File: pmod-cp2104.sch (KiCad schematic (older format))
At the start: 41 parts, among them P1 PMOD-CONN_6X2, P2 USB_OTG, SW1 SW_PUSH, U1 CP2104

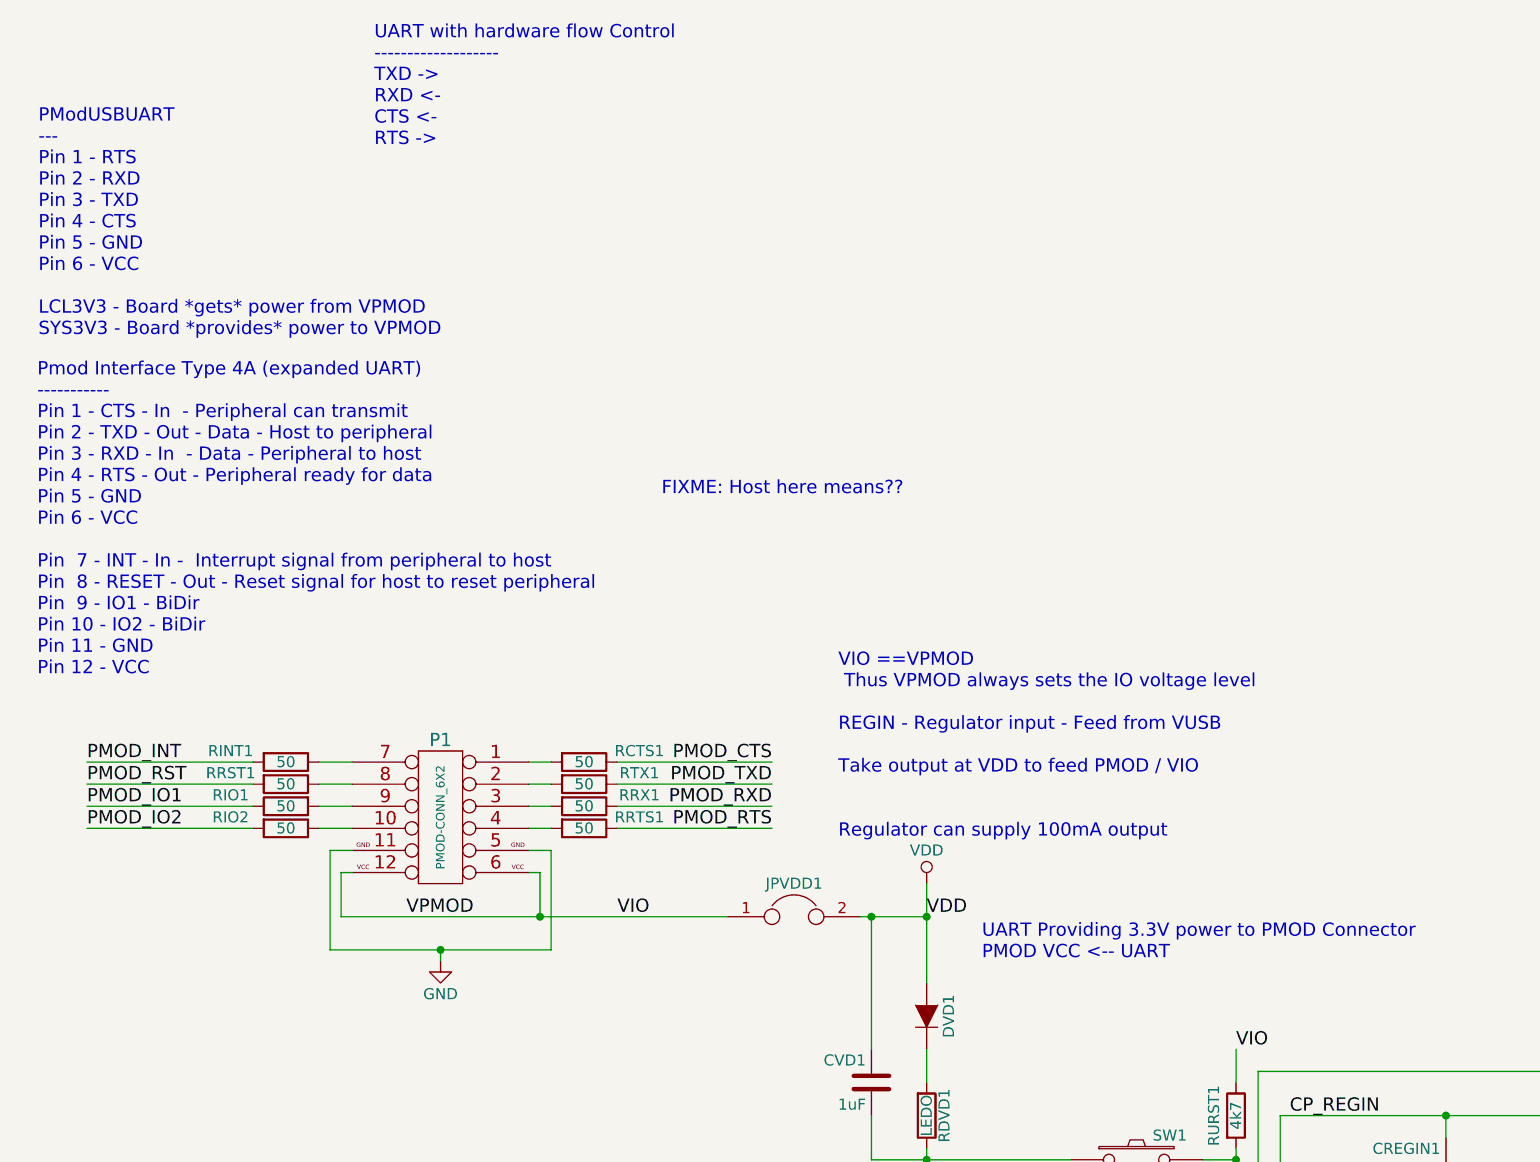
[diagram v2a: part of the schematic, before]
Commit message: Changing to using the pmod library.
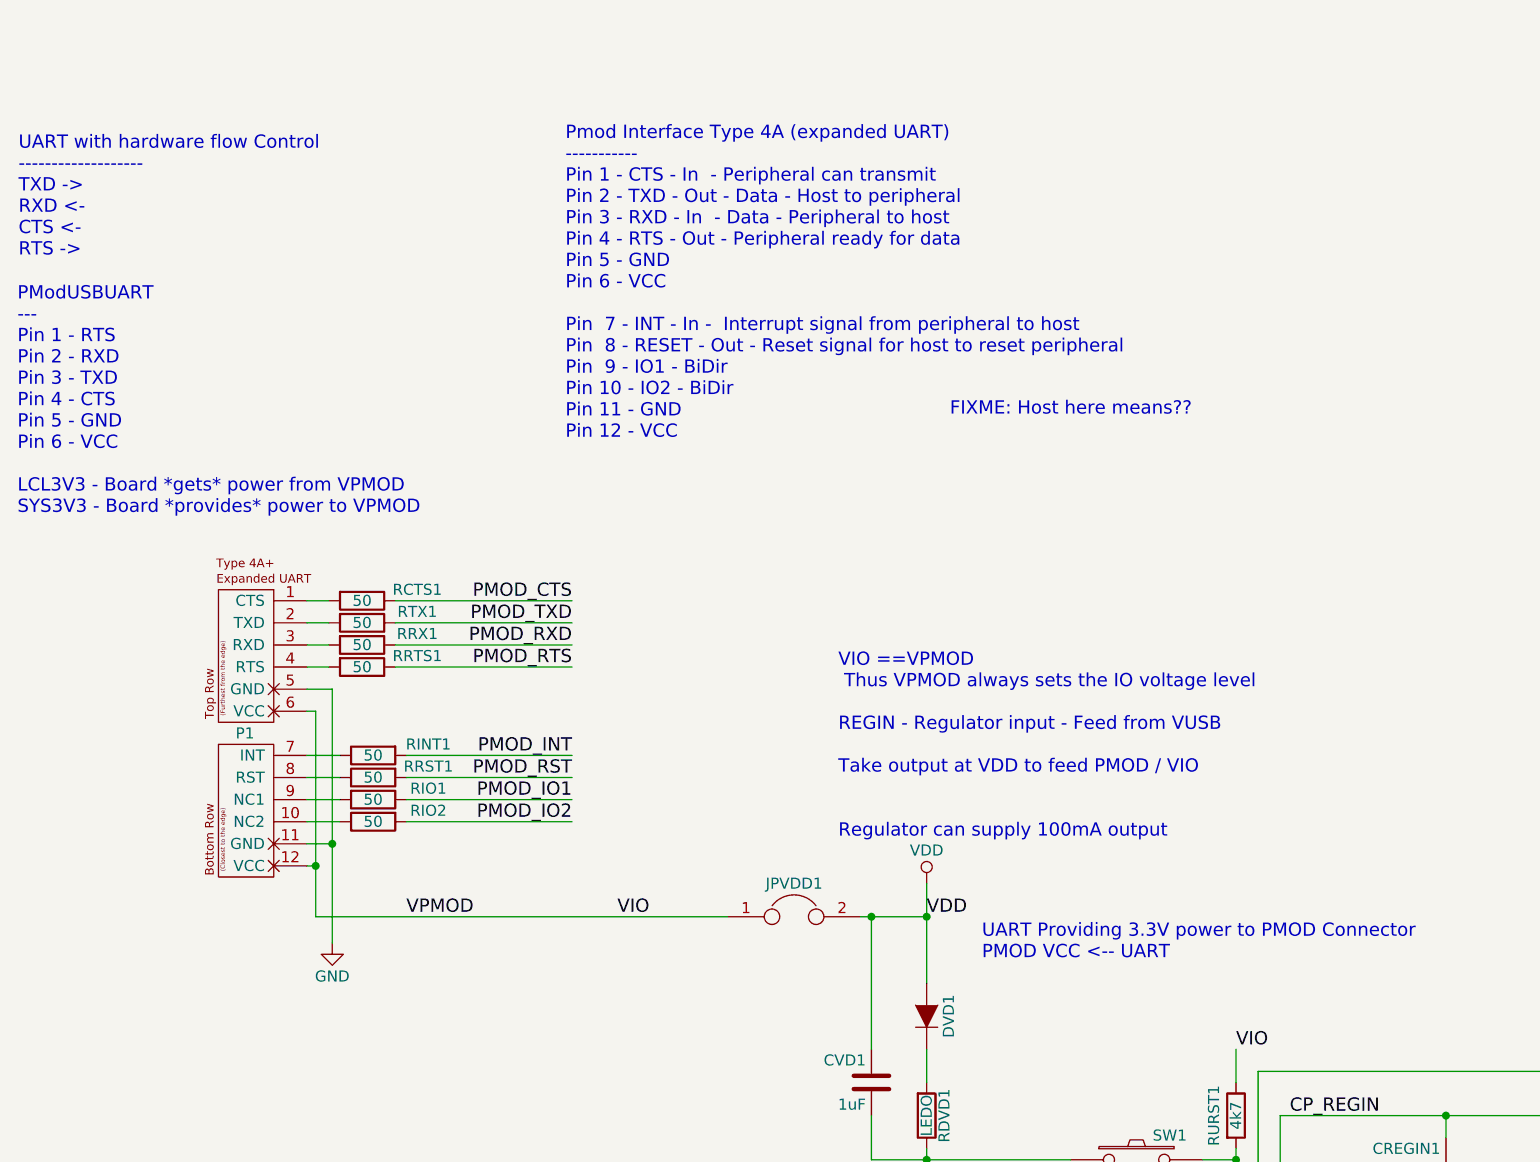
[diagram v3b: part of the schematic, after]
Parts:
- removed P1: PMOD-CONN_6X2, Pin_Headers:Pin_Header_Angled_2x06, symbol PMOD-CONN_6X2
- added P1: PMOD-Device-x2-Type-4A+-Expanded-UART, pmod-conn_6x2:pmod_pin_array_6x2, symbol PMOD-Device-x2-Type-4A+-Expanded-UART
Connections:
- net GND: now also P1.11 (GND), P1.5 (GND)
- net VIO: now also P1.12 (VCC), P1.6 (VCC)
- net at RCTS1.2: now also P1.1 (CTS)
- net at RIO2.1: now also P1.10 (NC2)
- net at RTX1.2: now also P1.2 (TXD)
- net at RRX1.2: now also P1.3 (RXD)
- net at RRTS1.2: now also P1.4 (RTS)
- net at RINT1.1: now also P1.7 (INT)
- net at RRST1.1: now also P1.8 (RST)
- net at RIO1.2: now also P1.9 (NC1)
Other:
- moved on the sheet: RCTS1, RINT1, RIO1, RIO2, RRST1, RRTS1, RRX1, RTX1
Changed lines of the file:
@@
 LIBS:contrib
 LIBS:valves
-LIBS:pmod-conn_6x2
 LIBS:cp2104
+LIBS:pmod
 LIBS:pmod-cp2104-cache
 EELAYER 25 0
@@
 Comment4 ""
 $EndDescr
-$Comp
-L PMOD-CONN_6X2 P1
-U 1 1 57F4CF0B
-P 2690 4475
-F 0 "P1" H 2690 4825 60  0000 C CNN
-F 1 "PMOD-CONN_6X2" V 2690 4475 39  0000 C CNN
-F 2 "Pin_Headers:Pin_Header_Angled_2x06" H 2690 4475 60  0001 C CNN
-F 3 "" H 2690 4475 60  0000 C CNN
-	1    2690 4475
-	-1   0    0    -1
-$EndComp
-Text Notes 2390 1445 0    60   ~ 0
+Text Notes 780  1945 0    60   ~ 0
 UART with hardware flow Control\n-------------------\nTXD ->\nRXD <-\nCTS <-\nRTS ->\n
 $Comp
@@
 	1    0    0    1
 $EndComp
-Text Notes 865  3840 0    60   ~ 0
+Text Notes 3255 2770 0    60   ~ 0
 Pmod Interface Type 4A (expanded UART) \n-----------\nPin 1 - CTS - In  - Peripheral can transmit\nPin 2 - TXD - Out - Data - Host to peripheral\nPin 3 - RXD - In  - Data - Peripheral to host\nPin 4 - RTS - Out - Peripheral ready for data\nPin 5 - GND\nPin 6 - VCC\n\nPin  7 - INT - In -  Interrupt signal from peripheral to host \nPin  8 - RESET - Out - Reset signal for host to reset peripheral \nPin  9 - IO1 - BiDir\nPin 10 - IO2 - BiDir\nPin 11 - GND\nPin 12 - VCC
-Text Label 4190 4225 2    60   ~ 0
+Text Label 3285 3495 2    60   ~ 0
 PMOD_CTS
-Text Label 4190 4325 2    60   ~ 0
+Text Label 3285 3595 2    60   ~ 0
 PMOD_TXD
-Text Label 4190 4425 2    60   ~ 0
+Text Label 3285 3695 2    60   ~ 0
 PMOD_RXD
-Text Label 4190 4525 2    60   ~ 0
+Text Label 3285 3795 2    60   ~ 0
 PMOD_RTS
-Text Label 1090 4225 0    60   ~ 0
+Text Label 3285 4195 2    60   ~ 0
 PMOD_INT
-Text Label 1090 4325 0    60   ~ 0
+Text Label 3285 4295 2    60   ~ 0
 PMOD_RST
-Text Label 1090 4425 0    60   ~ 0
+Text Label 3285 4395 2    60   ~ 0
 PMOD_IO1
-Text Label 1090 4525 0    60   ~ 0
+Text Label 3285 4495 2    60   ~ 0
 PMOD_IO2
 Text Label 8390 7225 0    60   ~ 0
@@
 L GND #PWR01
 U 1 1 57F4D651
-P 2690 5125
-F 0 "#PWR01" H 2690 4875 50  0001 C CNN
-F 1 "GND" H 2690 4975 50  0000 C CNN
-F 2 "" H 2690 5125 50  0000 C CNN
-F 3 "" H 2690 5125 50  0000 C CNN
-	1    2690 5125
+P 2200 5045
+F 0 "#PWR01" H 2200 4795 50  0001 C CNN
+F 1 "GND" H 2200 4895 50  0000 C CNN
+F 2 "" H 2200 5045 50  0000 C CNN
+F 3 "" H 2200 5045 50  0000 C CNN
+	1    2200 5045
 	-1   0    0    -1
 $EndComp
@@
 	1    0    0    -1
 $EndComp
-Text Notes 870  2305 0    60   ~ 0
+Text Notes 775  3110 0    60   ~ 0
 PModUSBUART\n---\nPin 1 - RTS\nPin 2 - RXD\nPin 3 - TXD\nPin 4 - CTS\nPin 5 - GND\nPin 6 - VCC\n\nLCL3V3 - Board *gets* power from VPMOD\nSYS3V3 - Board *provides* power to VPMOD
 Text Notes 4490 4575 0    60   ~ 0
@@
 L R RINT1
 U 1 1 57F500C7
-P 1990 4225
-F 0 "RINT1" V 1940 3975 50  0000 C CNN
-F 1 "50" V 1990 4225 50  0000 C CNN
-F 2 "Resistors_SMD:R_0603" V 1920 4225 50  0001 C CNN
-F 3 "" H 1990 4225 50  0000 C CNN
-	1    1990 4225
-	0    1    1    0
+P 2385 4195
+F 0 "RINT1" V 2335 3945 50  0000 C CNN
+F 1 "50" V 2385 4195 50  0000 C CNN
+F 2 "Resistors_SMD:R_0603" V 2315 4195 50  0001 C CNN
+F 3 "" H 2385 4195 50  0000 C CNN
+	1    2385 4195
+	0    -1   1    0
 $EndComp
 Text Label 11065 8015 0    60   ~ 0
@@
 L R RRST1
 U 1 1 57F52EB3
-P 1990 4325
-F 0 "RRST1" V 1940 4075 50  0000 C CNN
-F 1 "50" V 1990 4325 50  0000 C CNN
-F 2 "Resistors_SMD:R_0603" V 1920 4325 50  0001 C CNN
-F 3 "" H 1990 4325 50  0000 C CNN
-	1    1990 4325
-	0    1    1    0
+P 2385 4295
+F 0 "RRST1" V 2335 4045 50  0000 C CNN
+F 1 "50" V 2385 4295 50  0000 C CNN
+F 2 "Resistors_SMD:R_0603" V 2315 4295 50  0001 C CNN
+F 3 "" H 2385 4295 50  0000 C CNN
+	1    2385 4295
+	0    -1   1    0
 $EndComp
 $Comp
 L R RIO2
 U 1 1 57F53D72
-P 1990 4525
-F 0 "RIO2" V 1940 4275 50  0000 C CNN
-F 1 "50" V 1990 4525 50  0000 C CNN
-F 2 "Resistors_SMD:R_0603" V 1920 4525 50  0001 C CNN
-F 3 "" H 1990 4525 50  0000 C CNN
-	1    1990 4525
-	0    1    1    0
+P 2385 4495
+F 0 "RIO2" V 2335 4245 50  0000 C CNN
+F 1 "50" V 2385 4495 50  0000 C CNN
+F 2 "Resistors_SMD:R_0603" V 2315 4495 50  0001 C CNN
+F 3 "" H 2385 4495 50  0000 C CNN
+	1    2385 4495
+	0    -1   1    0
 $EndComp
 $Comp
 L R RTX1
 U 1 1 57F54253
-P 3340 4325
-F 0 "RTX1" V 3290 4575 50  0000 C CNN
-F 1 "50" V 3340 4325 50  0000 C CNN
-F 2 "Resistors_SMD:R_0603" V 3270 4325 50  0001 C CNN
-F 3 "" H 3340 4325 50  0000 C CNN
-	1    3340 4325
+P 2335 3595
+F 0 "RTX1" V 2285 3845 50  0000 C CNN
+F 1 "50" V 2335 3595 50  0000 C CNN
+F 2 "Resistors_SMD:R_0603" V 2265 3595 50  0001 C CNN
+F 3 "" H 2335 3595 50  0000 C CNN
+	1    2335 3595
 	0    1    1    0
 $EndComp
@@
 L R RRX1
 U 1 1 57F543D4
-P 3340 4425
-F 0 "RRX1" V 3290 4675 50  0000 C CNN
-F 1 "50" V 3340 4425 50  0000 C CNN
-F 2 "Resistors_SMD:R_0603" V 3270 4425 50  0001 C CNN
-F 3 "" H 3340 4425 50  0000 C CNN
-	1    3340 4425
+P 2335 3695
+F 0 "RRX1" V 2285 3945 50  0000 C CNN
+F 1 "50" V 2335 3695 50  0000 C CNN
+F 2 "Resistors_SMD:R_0603" V 2265 3695 50  0001 C CNN
+F 3 "" H 2335 3695 50  0000 C CNN
+	1    2335 3695
 	0    1    1    0
 $EndComp
@@
 L R RCTS1
 U 1 1 57F54490
-P 3340 4225
-F 0 "RCTS1" V 3290 4475 50  0000 C CNN
-F 1 "50" V 3340 4225 50  0000 C CNN
-F 2 "Resistors_SMD:R_0603" V 3270 4225 50  0001 C CNN
-F 3 "" H 3340 4225 50  0000 C CNN
-	1    3340 4225
+P 2335 3495
+F 0 "RCTS1" V 2285 3745 50  0000 C CNN
+F 1 "50" V 2335 3495 50  0000 C CNN
+F 2 "Resistors_SMD:R_0603" V 2265 3495 50  0001 C CNN
+F 3 "" H 2335 3495 50  0000 C CNN
+	1    2335 3495
 	0    1    1    0
 $EndComp
@@
 L R RRTS1
 U 1 1 57F545A3
-P 3340 4525
-F 0 "RRTS1" V 3290 4775 50  0000 C CNN
-F 1 "50" V 3340 4525 50  0000 C CNN
-F 2 "Resistors_SMD:R_0603" V 3270 4525 50  0001 C CNN
-F 3 "" H 3340 4525 50  0000 C CNN
-	1    3340 4525
+P 2335 3795
+F 0 "RRTS1" V 2285 4045 50  0000 C CNN
+F 1 "50" V 2335 3795 50  0000 C CNN
+F 2 "Resistors_SMD:R_0603" V 2265 3795 50  0001 C CNN
+F 3 "" H 2335 3795 50  0000 C CNN
+	1    2335 3795
 	0    1    1    0
 $EndComp
@@
 L R RIO1
 U 1 1 57F579B8
-P 1990 4425
-F 0 "RIO1" V 1940 4675 50  0000 C CNN
-F 1 "50" V 1990 4425 50  0000 C CNN
-F 2 "Resistors_SMD:R_0603" V 1920 4425 50  0001 C CNN
-F 3 "" H 1990 4425 50  0000 C CNN
-	1    1990 4425
-	0    -1   1    0
+P 2385 4395
+F 0 "RIO1" V 2335 4645 50  0000 C CNN
+F 1 "50" V 2385 4395 50  0000 C CNN
+F 2 "Resistors_SMD:R_0603" V 2315 4395 50  0001 C CNN
+F 3 "" H 2385 4395 50  0000 C CNN
+	1    2385 4395
+	0    1    1    0
 $EndComp
 $Comp
@@
 $EndComp
 Wire Wire Line
-	2290 4725 2240 4725
-Wire Wire Line
-	2240 4725 2240 4925
-Wire Wire Line
-	2240 4925 3990 4925
-Wire Wire Line
-	3140 4925 3140 4725
-Wire Wire Line
-	3140 4725 3090 4725
-Wire Wire Line
-	3090 4625 3190 4625
-Wire Wire Line
-	3190 4625 3190 5075
-Wire Wire Line
-	3190 5075 2190 5075
-Wire Wire Line
-	2190 5075 2190 4625
-Wire Wire Line
-	2190 4625 2290 4625
-Wire Wire Line
-	2690 5125 2690 5075
-Connection ~ 2690 5075
+	2125 4925 3990 4925
+Wire Wire Line
+	2200 3895 2200 5045
 Wire Wire Line
 	7990 7225 8740 7225
@@
 	12665 4515 12565 4515
 Wire Wire Line
-	3090 4225 3190 4225
-Wire Wire Line
-	3090 4325 3190 4325
-Wire Wire Line
-	3090 4425 3190 4425
-Wire Wire Line
-	3090 4525 3190 4525
-Wire Wire Line
-	3490 4225 4190 4225
-Wire Wire Line
-	4190 4325 3490 4325
-Wire Wire Line
-	3490 4425 4190 4425
-Wire Wire Line
-	4190 4525 3490 4525
-Wire Wire Line
-	2290 4225 2140 4225
-Wire Wire Line
-	2140 4325 2290 4325
-Wire Wire Line
-	2290 4425 2140 4425
-Wire Wire Line
-	2140 4525 2290 4525
-Wire Wire Line
-	1840 4225 1090 4225
-Wire Wire Line
-	1090 4325 1840 4325
-Wire Wire Line
-	1090 4425 1840 4425
-Wire Wire Line
-	1090 4525 1840 4525
-Connection ~ 3140 4925
+	2085 3495 2185 3495
+Wire Wire Line
+	2085 3595 2185 3595
+Wire Wire Line
+	2085 3695 2185 3695
+Wire Wire Line
+	2085 3795 2185 3795
+Wire Wire Line
+	2485 3495 3285 3495
+Wire Wire Line
+	3285 3595 2485 3595
+Wire Wire Line
+	2485 3695 3285 3695
+Wire Wire Line
+	3285 3795 2485 3795
+Wire Wire Line
+	2085 4195 2235 4195
+Wire Wire Line
+	2235 4295 2085 4295
+Wire Wire Line
+	2085 4395 2235 4395
+Wire Wire Line
+	2235 4495 2085 4495
+Wire Wire Line
+	2535 4195 3285 4195
+Wire Wire Line
+	3285 4295 2535 4295
+Wire Wire Line
+	3285 4395 2535 4395
+Wire Wire Line
+	3285 4495 2535 4495
 Wire Wire Line
 	4590 4925 4890 4925
@@
 Text Notes 10965 7865 2    60   ~ 0
 In <
-Text Notes 3690 3025 0    60   ~ 0
+Text Notes 4995 2665 0    60   ~ 0
 FIXME: Host here means??
 $Comp
@@
 	6140 6025 6290 6025
 Connection ~ 6290 6025
+Wire Wire Line
+	2125 3995 2125 4925
+Wire Wire Line
+	2125 4695 2085 4695
+Wire Wire Line
+	2200 4595 2085 4595
+Wire Wire Line
+	2200 3895 2085 3895
+Connection ~ 2200 4595
+Wire Wire Line
+	2085 3995 2125 3995
+Connection ~ 2125 4695
+$Comp
+L PMOD-Device-x2-Type-4A+-Expanded-UART P1
+U 1 1 583A9CC5
+P 1935 4045
+F 0 "P1" H 1805 3995 50  0000 C CNN
+F 1 "PMOD-Device-x2-Type-4A+-Expanded-UART" V 1575 3335 50  0001 L CNN
+F 2 "pmod-conn_6x2:pmod_pin_array_6x2" V 1485 3335 60  0001 L CNN
+F 3 "" H 1885 4345 60  0000 C CNN
+	1    1935 4045
+	1    0    0    -1
+$EndComp
 $EndSCHEMATC
